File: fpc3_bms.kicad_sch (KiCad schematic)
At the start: 2 parts, among them J2071 protected pack power, J2073 isolated bms control

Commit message: work on the power redesign and case
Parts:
- J2071: footprint Connector_Molex:Molex_Micro-Fit_3.0_43650-0224_1x02-1MP_P3.00mm_Vertical -> ducktop2:WAGO_2060_452_SMD; symbol Conn_01x02_MP:Conn_01x02_MP -> Connector_Generic:Conn_01x02; Contacts 43030-0038 tin, 18 awg; insulation diameter <=1.85 mm -> spring contact; CurrentRatingBasis PS-43650-001 N4: 2 circuits, 18 awg, 8.5 A at 30 C rise; va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 -> WAGO 2060, 9 A IEC/UL rating with 18 AWG; assembled tempera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; Harness 18 awg; pin 1 red; pin 2 black; straight-numbered; 75 mm le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 -> center: 1 FG_VSS, 2 PACK_POS_FUSED; BMS: 1 PACK_POS_FUSED, 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; MPN 43650-0224 -> 2060-452/998-404; Manufacturer Molex -> WAGO; MatedHeight reserve 17.56 mm per drawing, plus wire exit and bend -> 4.5 mm terminal body; reserve release-tool access; MatingHousing 43645-0200 -> bare wire; Wire (none) -> Alpha 6715 RD005/BK005, 18 AWG; minimum bend radius 8.763 mm
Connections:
- net FG_VSS: now also J2071.1 (Pin_1); no longer J2071.2 (Pin_2)
- net PACK_POS_FUSED: now also J2071.2 (Pin_2); no longer J2071.1 (Pin_1)
- no-connect marks 1 -> 0
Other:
- moved on the sheet: J2071
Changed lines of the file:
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@@
   (effects (font (size 1.27 1.27)) (justify left bottom))
 )
+(text "j2071 carries pack current through the rated power harness. j2073 supplies the isolated control island and its own return." (at 30.48 190.5 0) (effects (font (size 1.27 1.27))))
+(text "the bms control return never joins raw pack negative or the protected power return. the power return still crosses the center gauge shunt." (at 30.48 199.39 0) (effects (font (size 1.27 1.27))))
+(sheet_instances
+  (path "/46b21d0a-abb0-598b-9ae3-ea30d11d7d3c"
+    (page "16")
+  )
+)
+  (embedded_fonts no)
 (symbol
-  (lib_id "Conn_01x02_MP:Conn_01x02_MP")
+  (lib_id "Connector_Generic:Conn_01x02")
   (at 80.01 144.78 0)
   (unit 1)
@@
   (property "Reference" "J2071" (at 80.01 135.89 0) (effects (font (size 1.27 1.27))))
   (property "Value" "protected pack power" (at 80.01 153.67 0) (effects (font (size 1.27 1.27))))
-  (property "Footprint" "Connector_Molex:Molex_Micro-Fit_3.0_43650-0224_1x02-1MP_P3.00mm_Vertical" (at 80.01 144.78 0) (effects (font (size 1.27 1.27)) (hide yes)))
+  (property "Footprint" "ducktop2:WAGO_2060_452_SMD" (at 80.01 144.78 0) (effects (font (size 1.27 1.27)) (hide yes)))
   (property "Datasheet" "" (at 80.01 144.78 0) (effects (font (size 1.27 1.27)) (hide yes)))
-  (property "Manufacturer" "Molex" (at 80.01 144.78 0) (effects (font (size 1.27 1.27)) (hide yes)))
-  (property "MPN" "43650-0224" (at 80.01 144.78 0) (effects (font (size 1.27 1.27)) (hide yes)))
-  (property "MatingHousing" "43645-0200" (at 80.01 144.78 0) (effects (font (size 1.27 1.27)) (hide yes)))
-  (property "Harness" "18 awg; pin 1 red; pin 2 black; straight-numbered; 75 mm length budget" (at 80.01 144.78 0) (effects (font (size 1.27 1.27)) (hide yes)))
-  (property "Contacts" "43030-0038 tin, 18 awg; insulation diameter <=1.85 mm" (at 80.01 144.78 0) (effects (font (size 1.27 1.27)) (hide yes)))
-  (property "MatedHeight" "reserve 17.56 mm per drawing, plus wire exit and bend" (at 80.01 144.78 0) (effects (font (size 1.27 1.27)) (hide yes)))
-  (property "CurrentRatingBasis" "PS-43650-001 N4: 2 circuits, 18 awg, 8.5 A at 30 C rise; validate assembled temperature rise" (at 80.01 144.78 0) (effects (font (size 1.27 1.27)) (hide yes)))
-  (property "Datasheet" "https://www.molex.com/en-us/products/part-detail/0436500224" (at 80.01 144.78 0) (effects (font (size 1.27 1.27)) (hide yes)))
+  (property "Manufacturer" "WAGO" (at 80.01 144.78 0) (effects (font (size 1.27 1.27)) (hide yes)))
+  (property "MPN" "2060-452/998-404" (at 80.01 144.78 0) (effects (font (size 1.27 1.27)) (hide yes)))
+  (property "MatingHousing" "bare wire" (at 80.01 144.78 0) (effects (font (size 1.27 1.27)) (hide yes)))
+  (property "Contacts" "spring contact" (at 80.01 144.78 0) (effects (font (size 1.27 1.27)) (hide yes)))
+  (property "Wire" "Alpha 6715 RD005/BK005, 18 AWG; minimum bend radius 8.763 mm" (at 80.01 144.78 0) (effects (font (size 1.27 1.27)) (hide yes)))
+  (property "Harness" "center: 1 FG_VSS, 2 PACK_POS_FUSED; BMS: 1 PACK_POS_FUSED, 2 FG_VSS" (at 80.01 144.78 0) (effects (font (size 1.27 1.27)) (hide yes)))
+  (property "MatedHeight" "4.5 mm terminal body; reserve release-tool access" (at 80.01 144.78 0) (effects (font (size 1.27 1.27)) (hide yes)))
+  (property "CurrentRatingBasis" "WAGO 2060, 9 A IEC/UL rating with 18 AWG; assembled temperature still needs testing" (at 80.01 144.78 0) (effects (font (size 1.27 1.27)) (hide yes)))
+  (property "Datasheet" "https://www.wago.com/2060-452/998-404" (at 80.01 144.78 0) (effects (font (size 1.27 1.27)) (hide yes)))
   (pin "1")
   (pin "2")
-  (pin "MP")
   (instances
     (project "ducktop2"
@@
   )
 )
-(hierarchical_label "PACK_POS_FUSED"
+(hierarchical_label "FG_VSS"
   (shape bidirectional)
   (at 74.93 144.78 180)
   (effects (font (size 1.27 1.27)) (justify right bottom))
 )
-(hierarchical_label "FG_VSS"
+(hierarchical_label "PACK_POS_FUSED"
   (shape bidirectional)
   (at 74.93 147.32 180)
   (effects (font (size 1.27 1.27)) (justify right bottom))
 )
-(no_connect (at 85.09 146.05))
-(text "j2071 carries pack current through the rated power harness. j2073 supplies the isolated control island and its own return." (at 30.48 190.5 0) (effects (font (size 1.27 1.27))))
-(text "the bms control return never joins raw pack negative or the protected power return. the power return still crosses the center gauge shunt." (at 30.48 199.39 0) (effects (font (size 1.27 1.27))))
-(sheet_instances
-  (path "/46b21d0a-abb0-598b-9ae3-ea30d11d7d3c"
-    (page "16")
-  )
 )
-  (embedded_fonts no)
-)

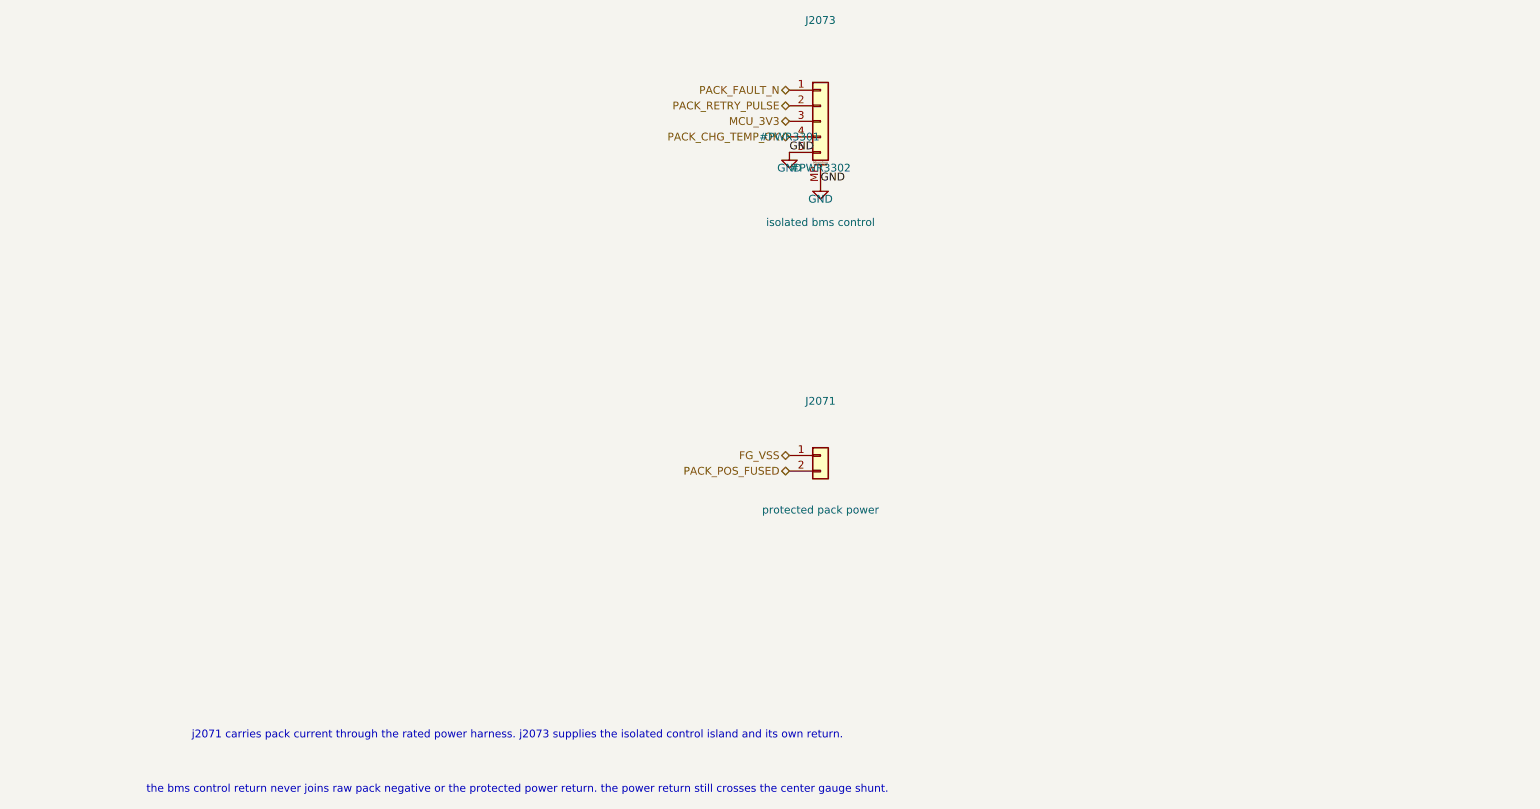
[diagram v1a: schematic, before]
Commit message: finish the new bms and move the connectors up top
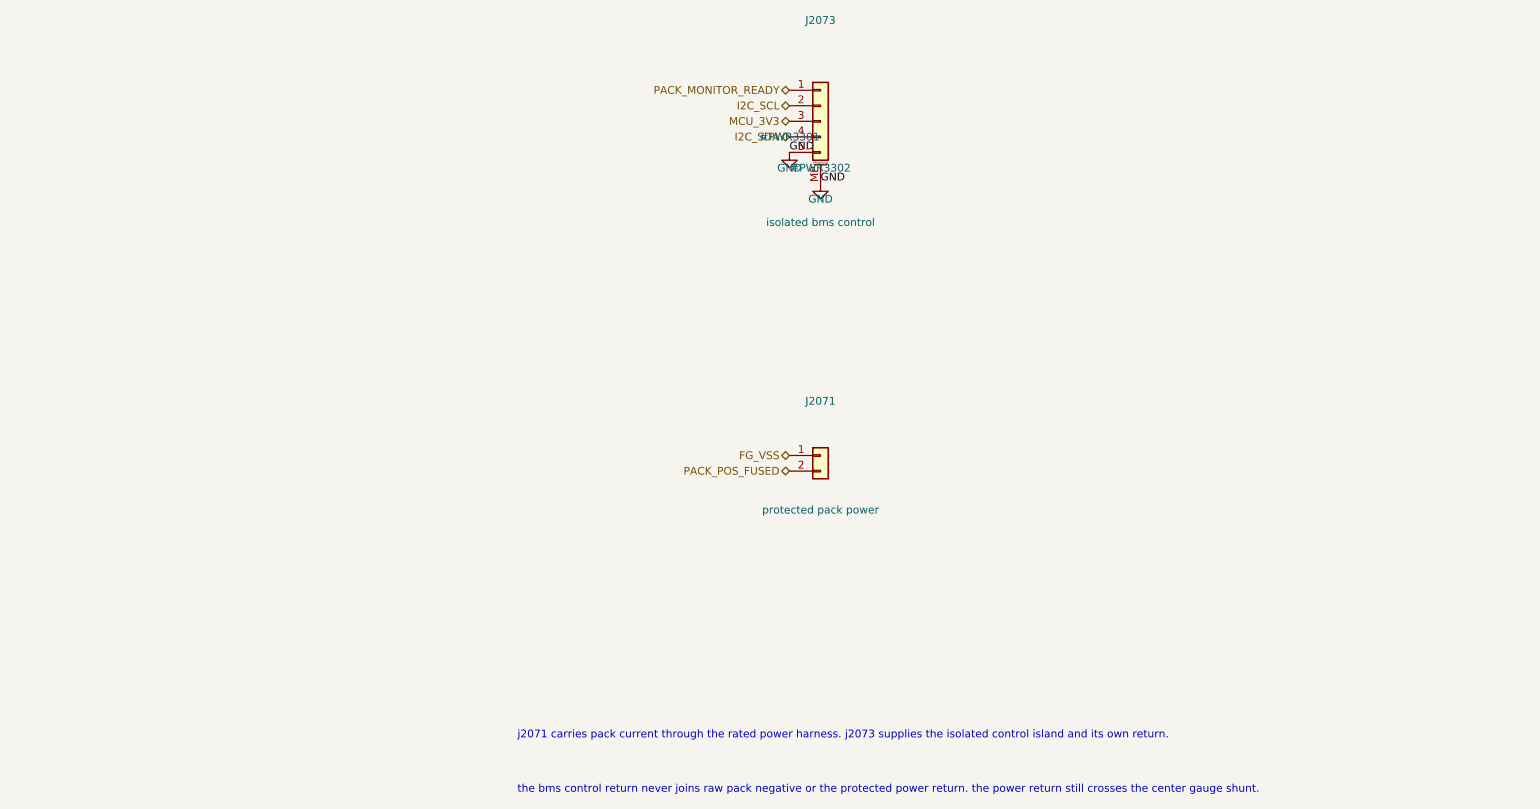
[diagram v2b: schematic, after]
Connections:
- net PACK_CHG_TEMP_OK renamed I2C_SDA
- net PACK_FAULT_N renamed PACK_MONITOR_READY
- net PACK_RETRY_PULSE renamed I2C_SCL
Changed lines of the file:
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@@
   )
 )
-(hierarchical_label "PACK_FAULT_N"
+(hierarchical_label "PACK_MONITOR_READY"
   (shape bidirectional)
   (at 74.93 85.09 180)
   (effects (font (size 1.27 1.27)) (justify right bottom))
 )
-(hierarchical_label "PACK_RETRY_PULSE"
+(hierarchical_label "I2C_SCL"
   (shape bidirectional)
   (at 74.93 87.63 180)
@@
   (effects (font (size 1.27 1.27)) (justify right bottom))
 )
-(hierarchical_label "PACK_CHG_TEMP_OK"
+(hierarchical_label "I2C_SDA"
   (shape bidirectional)
   (at 74.93 92.71 180)
@@
   (effects (font (size 1.27 1.27)) (justify left bottom))
 )
-(text "j2071 carries pack current through the rated power harness. j2073 supplies the isolated control island and its own return." (at 30.48 190.5 0) (effects (font (size 1.27 1.27))))
-(text "the bms control return never joins raw pack negative or the protected power return. the power return still crosses the center gauge shunt." (at 30.48 199.39 0) (effects (font (size 1.27 1.27))))
-(sheet_instances
-  (path "/46b21d0a-abb0-598b-9ae3-ea30d11d7d3c"
-    (page "16")
-  )
-)
-  (embedded_fonts no)
 (symbol
   (lib_id "Connector_Generic:Conn_01x02")
@@
   (effects (font (size 1.27 1.27)) (justify right bottom))
 )
+(text "j2071 carries pack current through the rated power harness. j2073 supplies the isolated control island and its own return." (at 30.48 190.5 0) (effects (font (size 1.27 1.27)) (justify left)))
+(text "the bms control return never joins raw pack negative or the protected power return. the power return still crosses the center gauge shunt." (at 30.48 199.39 0) (effects (font (size 1.27 1.27)) (justify left)))
+(sheet_instances
+  (path "/46b21d0a-abb0-598b-9ae3-ea30d11d7d3c"
+    (page "16")
+  )
 )
+  (embedded_fonts no)
+)
